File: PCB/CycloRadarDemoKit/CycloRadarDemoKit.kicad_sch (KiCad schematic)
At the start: 17 parts, among them J101 JTAG, SW101 RESET, SW102 BOOT MODE, U101 ESP32-WROVER-E

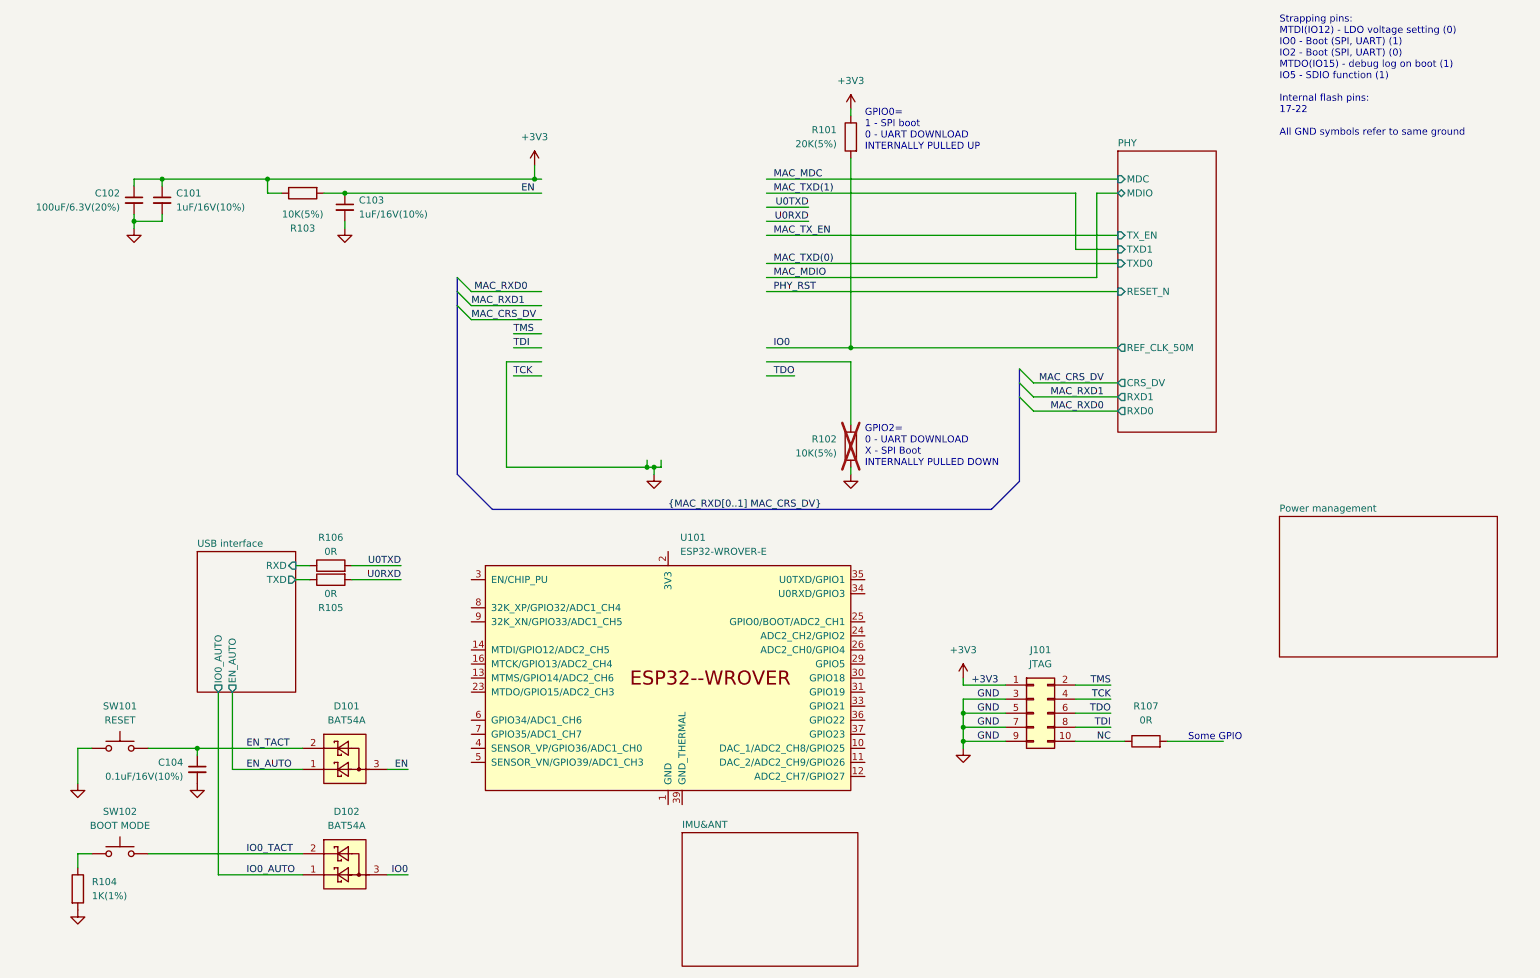
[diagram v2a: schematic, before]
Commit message: Readme, PCB new symbol routed
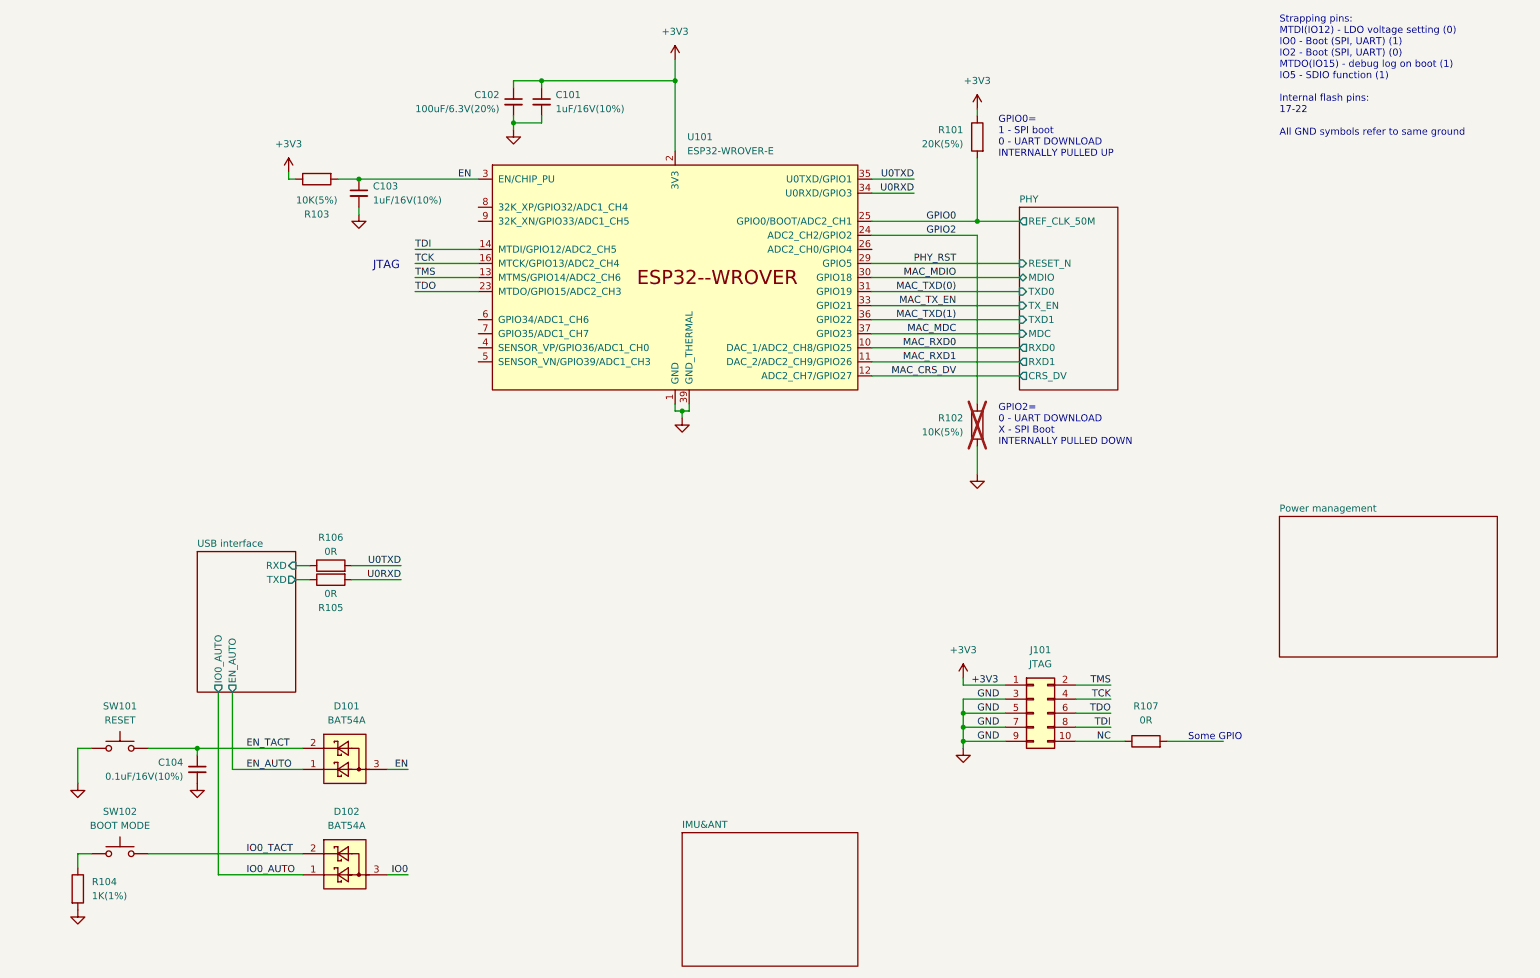
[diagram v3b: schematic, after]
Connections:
- net +3V3: now also U101.2 (3V3)
- net EN: now also U101.3 (EN/CHIP_PU)
- net GND: now also U101.1 (GND), U101.15 (GND), U101.38 (GND), U101.39 (GND_THERMAL)
- net IO0: no longer R101.2
- net MAC_CRS_DV: now also U101.12 (ADC2_CH7/GPIO27)
- net MAC_MDC: now also U101.37 (GPIO23)
- net MAC_MDIO: now also U101.30 (GPIO18)
- net MAC_RXD0: now also U101.10 (DAC_1/ADC2_CH8/GPIO25)
- net MAC_RXD1: now also U101.11 (DAC_2/ADC2_CH9/GPIO26)
- net MAC_TXD(0): now also U101.31 (GPIO19)
- net MAC_TXD(1): now also U101.36 (GPIO22)
- net MAC_TX_EN: now also U101.33 (GPIO21)
- net PHY_RST: now also U101.29 (GPIO5)
- net TCK: now also U101.16 (MTCK/GPIO13/ADC2_CH4)
- net TDI: now also U101.14 (MTDI/GPIO12/ADC2_CH5)
- net TDO: now also U101.23 (MTDO/GPIO15/ADC2_CH3)
- net TMS: now also U101.13 (MTMS/GPIO14/ADC2_CH6)
- net U0RXD: now also U101.34 (U0RXD/GPIO3)
- net U0TXD: now also U101.35 (U0TXD/GPIO1)
- net GPIO2: now reaches R102.1
- net GPIO2: now also U101.24 (ADC2_CH2/GPIO2)
- net GPIO0: now reaches U101.25 (GPIO0/BOOT/ADC2_CH1)
- net GPIO0: now also R101.2
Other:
- note added: "JTAG"
- moved on the sheet: C101, C102, C103, R101, R102, R103, U101

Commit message: PCB power manag. WIP
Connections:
- net GPIO0 renamed MAC_CLK
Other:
- sheet Power management ports: added 12V_EN; removed none
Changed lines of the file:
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@@
     (stroke (width 0) (type default))
   )
-  (wire (pts (xy 186.69 96.52) (xy 186.69 101.6))
+  (wire (pts (xy 186.69 97.79) (xy 186.69 96.52))
     (stroke (width 0) (type default))
   )
@@
     (stroke (width 0) (type default))
   )
-  (wire (pts (xy 132.08 26.67) (xy 132.08 30.48))
+  (wire (pts (xy 132.08 29.21) (xy 132.08 30.48))
     (stroke (width 0) (type default))
   )
@@
   )
   (wire (pts (xy 134.62 88.9) (xy 134.62 90.17))
-    (stroke (width 0) (type default))
-  )
-  (wire (pts (xy 186.69 35.56) (xy 186.69 36.83))
     (stroke (width 0) (type default))
   )
@@
     (effects (font (size 1.27 1.27)) (justify right bottom))
   )
-  (label "GPIO0" (at 182.88 55.88 180) (fields_autoplaced)
+  (label "MAC_CLK" (at 182.88 55.88 180) (fields_autoplaced)
     (effects (font (size 1.27 1.27)) (justify right bottom))
   )
@@
     )
   )
-  (symbol (lib_id "power:+3V3") (at 186.69 35.56 0) (unit 1)
-    (in_bom yes) (on_board yes) (dnp no) (fields_autoplaced)
-    (property "Reference" "#PWR0101" (at 186.69 39.37 0)
-      (effects (font (size 1.27 1.27)) hide)
-    )
-    (property "Value" "+3V3" (at 186.69 30.48 0)
-      (effects (font (size 1.27 1.27)))
-    )
-    (property "Footprint" "" (at 186.69 35.56 0)
-      (effects (font (size 1.27 1.27)) hide)
-    )
-    (property "Datasheet" "" (at 186.69 35.56 0)
+  (symbol (lib_id "power:+3V3") (at 186.69 36.83 0) (unit 1)
+    (in_bom yes) (on_board yes) (dnp no) (fields_autoplaced)
+    (property "Reference" "#PWR0101" (at 186.69 40.64 0)
+      (effects (font (size 1.27 1.27)) hide)
+    )
+    (property "Value" "+3V3" (at 186.69 31.75 0)
+      (effects (font (size 1.27 1.27)))
+    )
+    (property "Footprint" "" (at 186.69 36.83 0)
+      (effects (font (size 1.27 1.27)) hide)
+    )
+    (property "Datasheet" "" (at 186.69 36.83 0)
       (effects (font (size 1.27 1.27)) hide)
     )
@@
     )
   )
-  (symbol (lib_id "power:+3V3") (at 132.08 26.67 0) (unit 1)
-    (in_bom yes) (on_board yes) (dnp no) (fields_autoplaced)
-    (property "Reference" "#PWR0103" (at 132.08 30.48 0)
-      (effects (font (size 1.27 1.27)) hide)
-    )
-    (property "Value" "+3V3" (at 132.08 21.59 0)
-      (effects (font (size 1.27 1.27)))
-    )
-    (property "Footprint" "" (at 132.08 26.67 0)
-      (effects (font (size 1.27 1.27)) hide)
-    )
-    (property "Datasheet" "" (at 132.08 26.67 0)
+  (symbol (lib_id "power:+3V3") (at 132.08 29.21 0) (unit 1)
+    (in_bom yes) (on_board yes) (dnp no) (fields_autoplaced)
+    (property "Reference" "#PWR0103" (at 132.08 33.02 0)
+      (effects (font (size 1.27 1.27)) hide)
+    )
+    (property "Value" "+3V3" (at 132.08 24.13 0)
+      (effects (font (size 1.27 1.27)))
+    )
+    (property "Footprint" "" (at 132.08 29.21 0)
+      (effects (font (size 1.27 1.27)) hide)
+    )
+    (property "Datasheet" "" (at 132.08 29.21 0)
       (effects (font (size 1.27 1.27)) hide)
     )
@@
     )
   )
-  (symbol (lib_id "power:GND") (at 186.69 101.6 0) (unit 1)
-    (in_bom yes) (on_board yes) (dnp no) (fields_autoplaced)
-    (property "Reference" "#PWR0102" (at 186.69 107.95 0)
-      (effects (font (size 1.27 1.27)) hide)
-    )
-    (property "Value" "GND" (at 186.69 106.68 0)
-      (effects (font (size 1.27 1.27)) hide)
-    )
-    (property "Footprint" "" (at 186.69 101.6 0)
-      (effects (font (size 1.27 1.27)) hide)
-    )
-    (property "Datasheet" "" (at 186.69 101.6 0)
+  (symbol (lib_id "power:GND") (at 186.69 97.79 0) (unit 1)
+    (in_bom yes) (on_board yes) (dnp no) (fields_autoplaced)
+    (property "Reference" "#PWR0102" (at 186.69 104.14 0)
+      (effects (font (size 1.27 1.27)) hide)
+    )
+    (property "Value" "GND" (at 186.69 102.87 0)
+      (effects (font (size 1.27 1.27)) hide)
+    )
+    (property "Footprint" "" (at 186.69 97.79 0)
+      (effects (font (size 1.27 1.27)) hide)
+    )
+    (property "Datasheet" "" (at 186.69 97.79 0)
       (effects (font (size 1.27 1.27)) hide)
     )
@@
     )
   )
-  (sheet (at 241.3 109.22) (size 39.37 25.4) (fields_autoplaced)
+  (sheet (at 231.14 104.14) (size 39.37 25.4) (fields_autoplaced)
     (stroke (width 0.1524) (type solid))
     (fill (color 0 0 0 0.1000))
-    (property "Sheetname" "Power management" (at 241.3 108.5084 0)
+    (property "Sheetname" "Power management" (at 231.14 103.4284 0)
       (effects (font (size 1.27 1.27)) (justify left bottom))
     )
-    (property "Sheetfile" "PM.kicad_sch" (at 241.3 135.2046 0)
+    (property "Sheetfile" "PM.kicad_sch" (at 231.14 130.1246 0)
       (effects (font (size 1.27 1.27)) (justify left top) hide)
     )
-    (instances
+    (pin "12V_EN" input (at 231.14 110.49 180)
+      (effects (font (size 1.27 1.27)) (justify left))
+    )
+    (instances

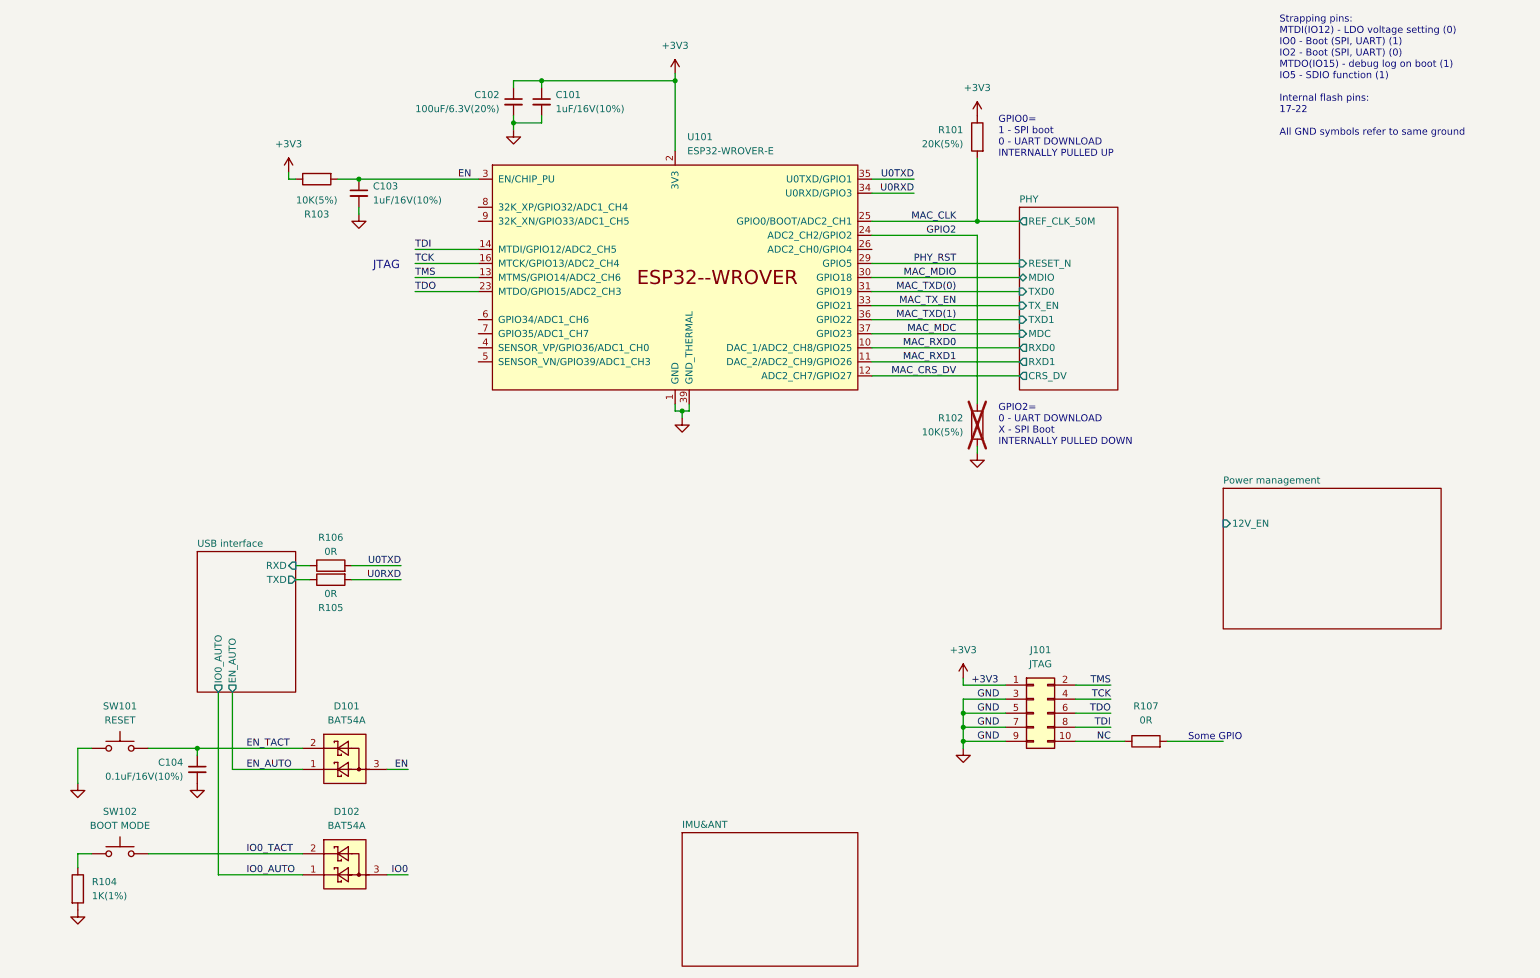
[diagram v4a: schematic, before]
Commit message: Power management almost done
5V/3.3V changed to AP63203
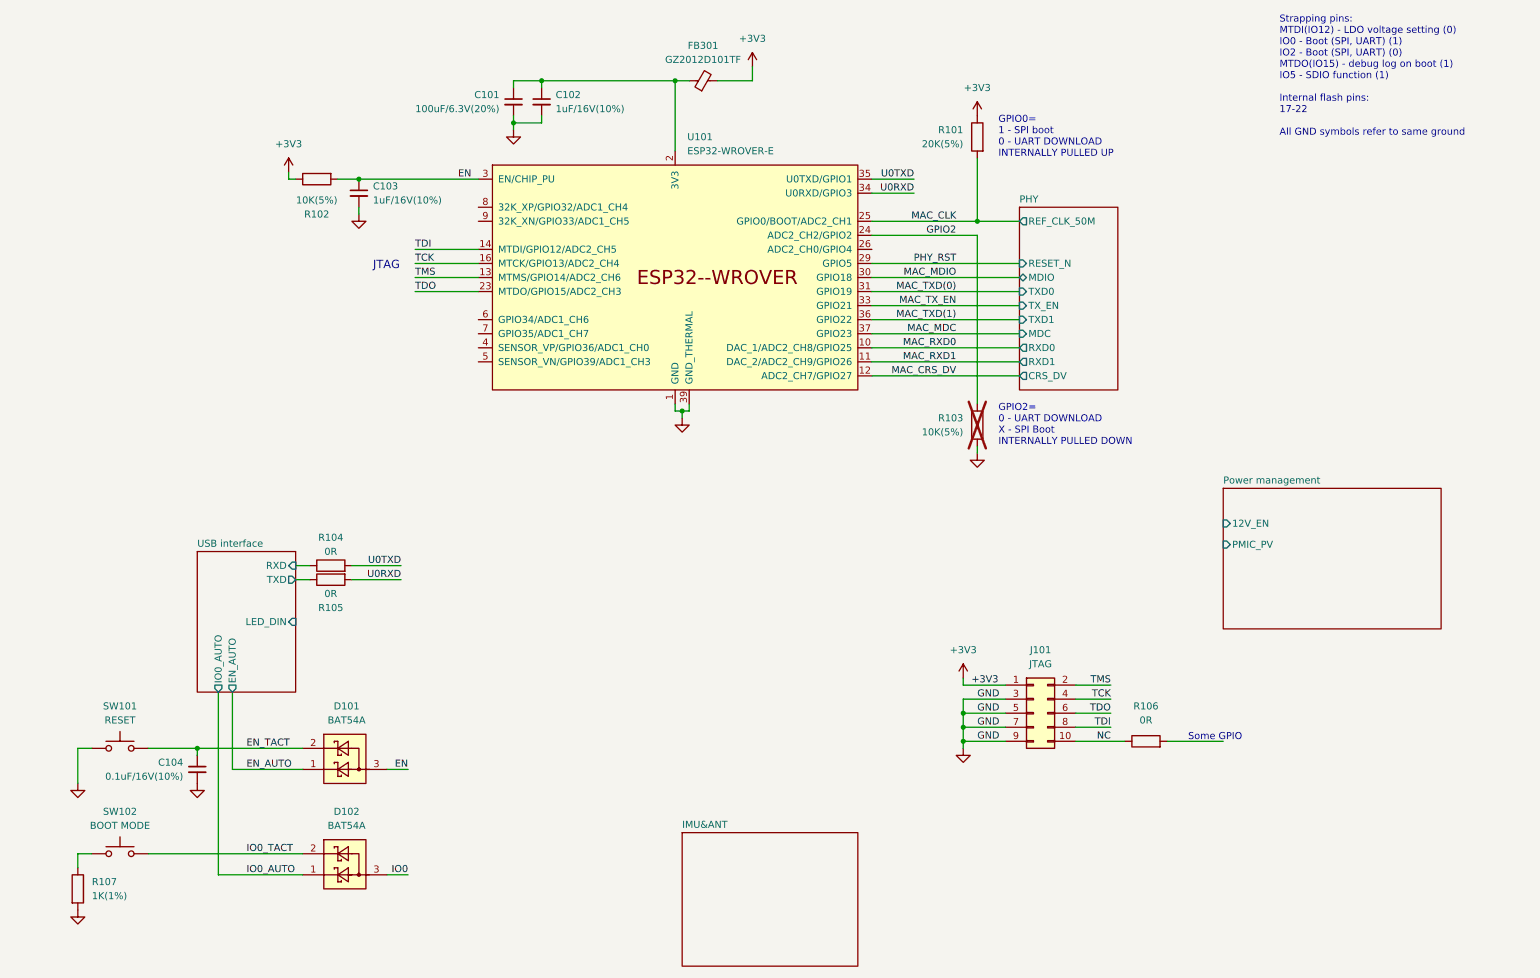
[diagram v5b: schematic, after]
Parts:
- added FB301: GZ2012D101TF, symbol Device:FerriteBead_Small
- renumbered C102 to C101, C101 to C102, R103 to R102, R102 to R103, R106 to R104, R107 to R106, R104 to R107
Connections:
- net +3V3: now also FB301.2; no longer C101.1, C102.1, U101.2 (3V3)
- new net: C101.1, C102.1, FB301.1, U101.2 (3V3)
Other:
- sheet Power management ports: added PMIC_PV; removed none
- sheet USB interface ports: added LED_DIN; removed none
